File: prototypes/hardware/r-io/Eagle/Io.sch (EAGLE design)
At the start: 87 parts, among them IC1 AT90CAN128, IC2 MCP2551SO8, IC3 NUP2105L, IC5 LD117ADT50TR, J1 POWER_JACKPTH, Q1 56P2859, Q2 PMV56XN, Q3 PMV56XN, Q4 PMV56XN, Q5 PMV56XN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

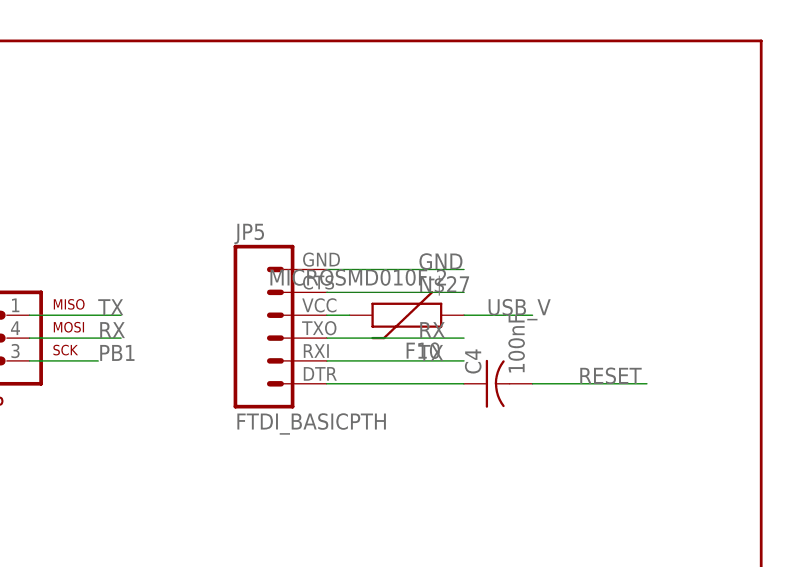
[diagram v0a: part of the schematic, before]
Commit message: Connected CTS on FTDI header to ground.
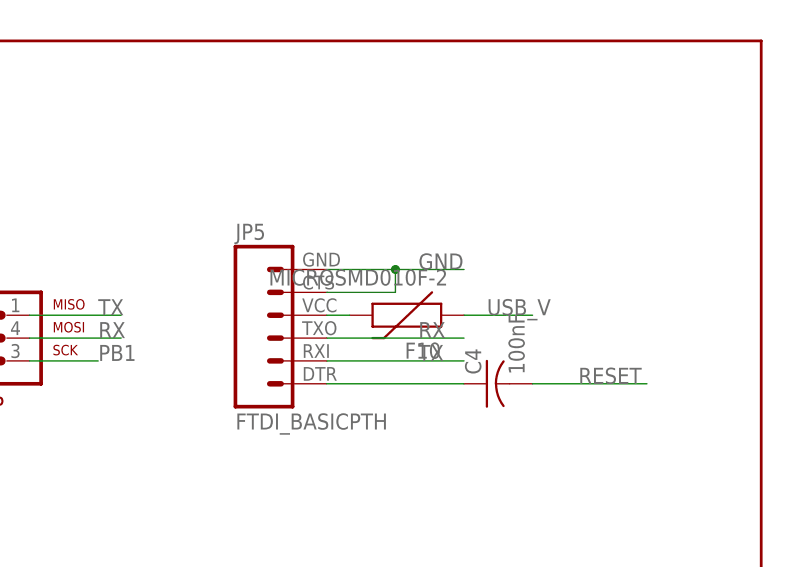
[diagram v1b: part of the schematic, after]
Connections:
- removed net N$27: JP5.5
- net GND: now also JP5.5
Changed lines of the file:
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@@
 </segment>
 <segment>
-<wire x1="-243.84" y1="160.02" x2="-228.6" y2="160.02" width="0.1524" layer="91"/>
+<wire x1="-243.84" y1="160.02" x2="-236.22" y2="160.02" width="0.1524" layer="91"/>
 <label x="-233.68" y="160.02" size="1.778" layer="95"/>
 <pinref part="JP5" gate="G$1" pin="6"/>
+<wire x1="-236.22" y1="160.02" x2="-228.6" y2="160.02" width="0.1524" layer="91"/>
+<wire x1="-243.84" y1="157.48" x2="-236.22" y2="157.48" width="0.1524" layer="91"/>
+<pinref part="JP5" gate="G$1" pin="5"/>
+<wire x1="-236.22" y1="157.48" x2="-236.22" y2="160.02" width="0.1524" layer="91"/>
+<junction x="-236.22" y="160.02"/>
 </segment>
 <segment>
@@
 </segment>
 </net>
-<net name="N$27" class="0">
-<segment>
-<wire x1="-243.84" y1="157.48" x2="-228.6" y2="157.48" width="0.1524" layer="91"/>
-<label x="-233.68" y="157.48" size="1.778" layer="95"/>
-<pinref part="JP5" gate="G$1" pin="5"/>
-</segment>
-</net>

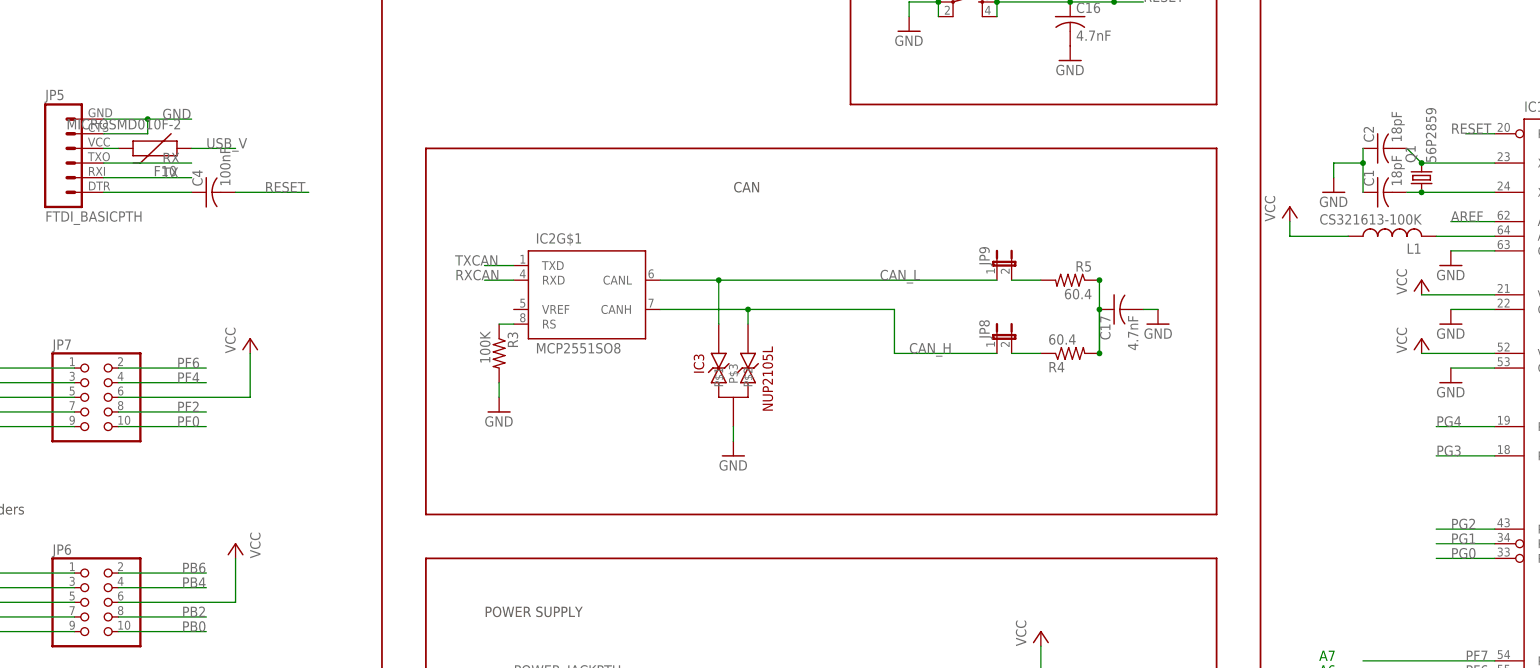
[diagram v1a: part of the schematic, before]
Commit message: Added default-on solder jumper for CTS line to ground. Added resistor/jumper pair for PG4—the only unused pin—to provide future configuration option.
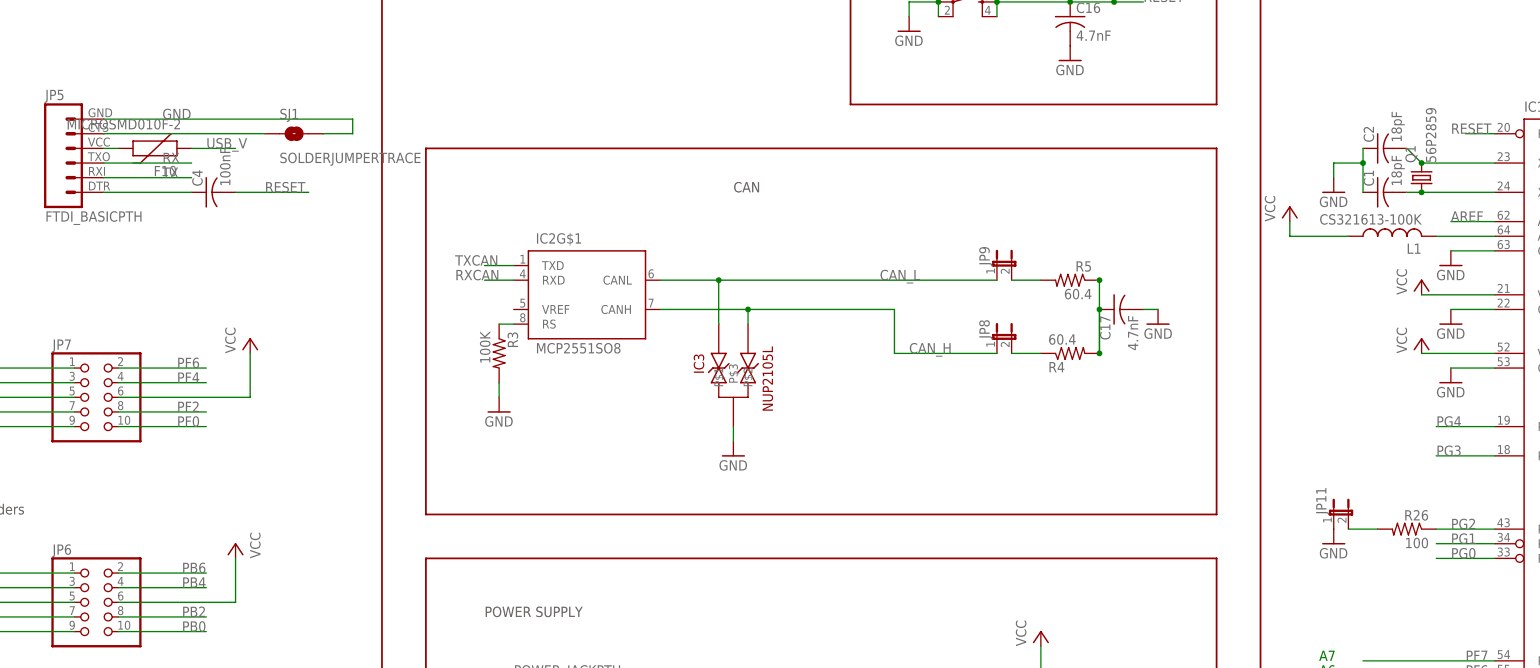
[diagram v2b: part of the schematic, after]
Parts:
- added JP11: (no value), SparkFun:JUMPER-2PTH
- added R26: 100, rcl:R-US_R1206
- added SJ1: SOLDERJUMPERTRACE, SparkFun:SOLDERJUMPERTRACE
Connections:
- new net N$23: JP5.5, SJ1.1
- new net N$25: JP11.2, R26.2
- net GND: now also JP11.1, SJ1.2; no longer JP5.5
- net PG2: now also R26.1
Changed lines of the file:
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@@
 <part name="LED11" library="led" deviceset="LED" device="CHIPLED_1206"/>
 <part name="L1" library="rcl" deviceset="L-US" device="L3216C" value="CS321613-100K"/>
+<part name="SJ1" library="SparkFun" deviceset="SOLDERJUMPER" device="TRACE"/>
+<part name="R26" library="rcl" deviceset="R-US_" device="R1206" value="100"/>
+<part name="JP11" library="SparkFun" deviceset="JUMPER-2" device="PTH"/>
+<part name="GND28" library="supply1" deviceset="GND" device=""/>
 </parts>
 <sheets>
@@
 <instance part="LED11" gate="G$1" x="-287.02" y="213.36" rot="R90"/>
 <instance part="L1" gate="G$1" x="-20.32" y="139.7" rot="R90"/>
+<instance part="SJ1" gate="1" x="-210.82" y="157.48"/>
+<instance part="R26" gate="G$1" x="-17.78" y="88.9" rot="MR0"/>
+<instance part="JP11" gate="A" x="-30.48" y="91.44"/>
+<instance part="GND28" gate="1" x="-30.48" y="86.36"/>
 </instances>
 <busses>
@@
 </segment>
 <segment>
-<wire x1="-243.84" y1="160.02" x2="-236.22" y2="160.02" width="0.1524" layer="91"/>
 <label x="-233.68" y="160.02" size="1.778" layer="95"/>
 <pinref part="JP5" gate="G$1" pin="6"/>
-<wire x1="-236.22" y1="160.02" x2="-228.6" y2="160.02" width="0.1524" layer="91"/>
-<wire x1="-243.84" y1="157.48" x2="-236.22" y2="157.48" width="0.1524" layer="91"/>
-<pinref part="JP5" gate="G$1" pin="5"/>
-<wire x1="-236.22" y1="157.48" x2="-236.22" y2="160.02" width="0.1524" layer="91"/>
-<junction x="-236.22" y="160.02"/>
+<pinref part="SJ1" gate="1" pin="2"/>
+<wire x1="-205.74" y1="157.48" x2="-200.66" y2="157.48" width="0.1524" layer="91"/>
+<wire x1="-200.66" y1="157.48" x2="-200.66" y2="160.02" width="0.1524" layer="91"/>
+<wire x1="-200.66" y1="160.02" x2="-243.84" y2="160.02" width="0.1524" layer="91"/>
 </segment>
 <segment>
@@
 <pinref part="GND2" gate="1" pin="GND"/>
 </segment>
+<segment>
+<pinref part="JP11" gate="A" pin="1"/>
+<pinref part="GND28" gate="1" pin="GND"/>
+</segment>
 </net>
 <net name="XTAL1" class="0">
@@
 <label x="-10.16" y="88.9" size="1.778" layer="95"/>
 <pinref part="IC1" gate="G$1" pin="PG2(ALE)"/>
+<pinref part="R26" gate="G$1" pin="1"/>
 </segment>
 </net>
@@
 </segment>
 </net>
+<net name="N$23" class="2">
+<segment>
+<pinref part="JP5" gate="G$1" pin="5"/>
+<pinref part="SJ1" gate="1" pin="1"/>
+<wire x1="-243.84" y1="157.48" x2="-215.9" y2="157.48" width="0.1524" layer="91"/>
+</segment>
+</net>
+<net name="N$25" class="0">
+<segment>
+<pinref part="R26" gate="G$1" pin="2"/>
+<pinref part="JP11" gate="A" pin="2"/>
+<wire x1="-27.94" y1="88.9" x2="-22.86" y2="88.9" width="0.1524" layer="91"/>
+</segment>
+</net>

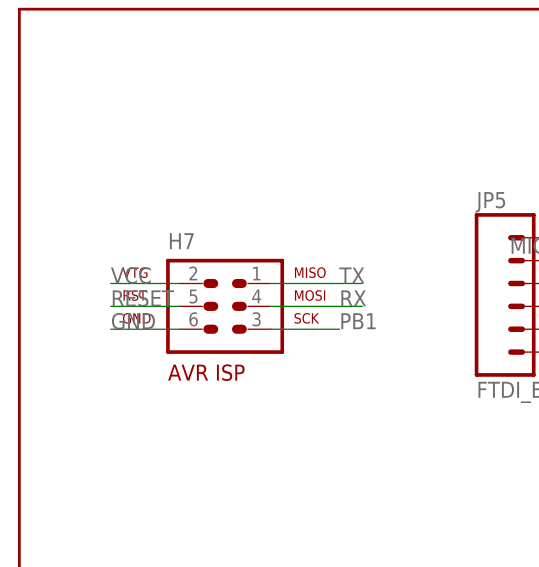
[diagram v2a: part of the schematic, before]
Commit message: Fattened up the labels.  Rerouted to avoid running under the crystal.  Moved Reset button slightly away from mounting hole.
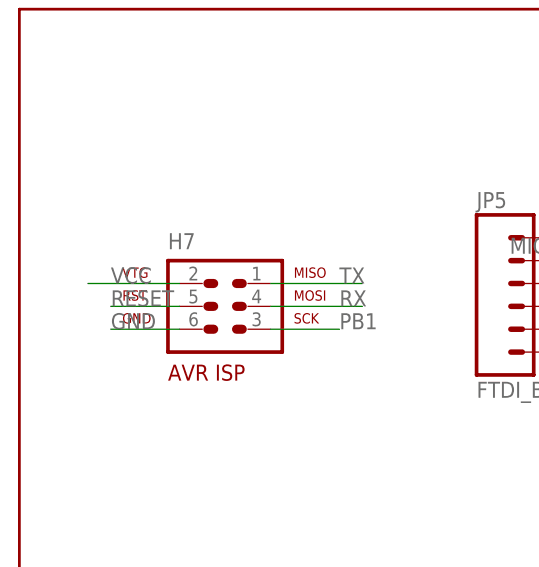
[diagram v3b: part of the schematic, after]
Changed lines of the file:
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@@
 <net name="VCC" class="0">
 <segment>
-<wire x1="-287.02" y1="154.94" x2="-294.64" y2="154.94" width="0.1524" layer="91"/>
+<wire x1="-287.02" y1="154.94" x2="-297.18" y2="154.94" width="0.1524" layer="91"/>
 <label x="-294.64" y="154.94" size="1.778" layer="95"/>
 <pinref part="H7" gate="G$1" pin="2"/>
